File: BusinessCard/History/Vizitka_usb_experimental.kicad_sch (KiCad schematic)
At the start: 29 parts, among them J1 USB_B_Micro, J2 USB_C_Receptacle, J3 Conn_01x01

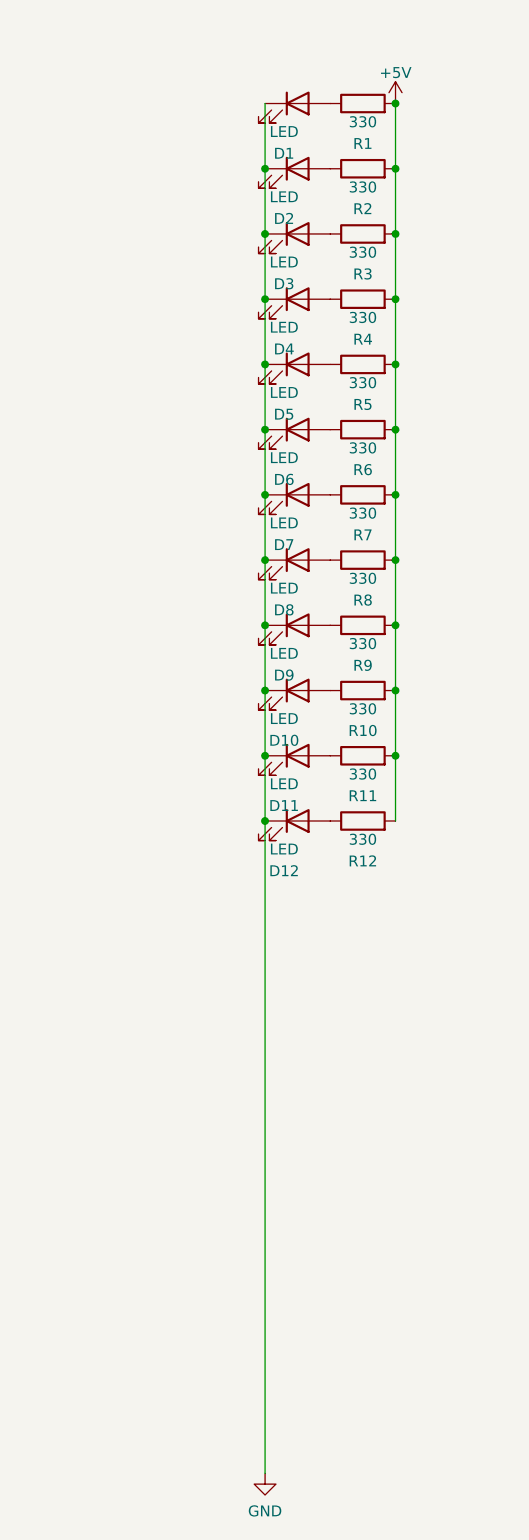
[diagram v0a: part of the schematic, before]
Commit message: Added aditional businesscards - Zuza, MichalModra...Actual Tapeout 2023-08-24, but repaired connection!
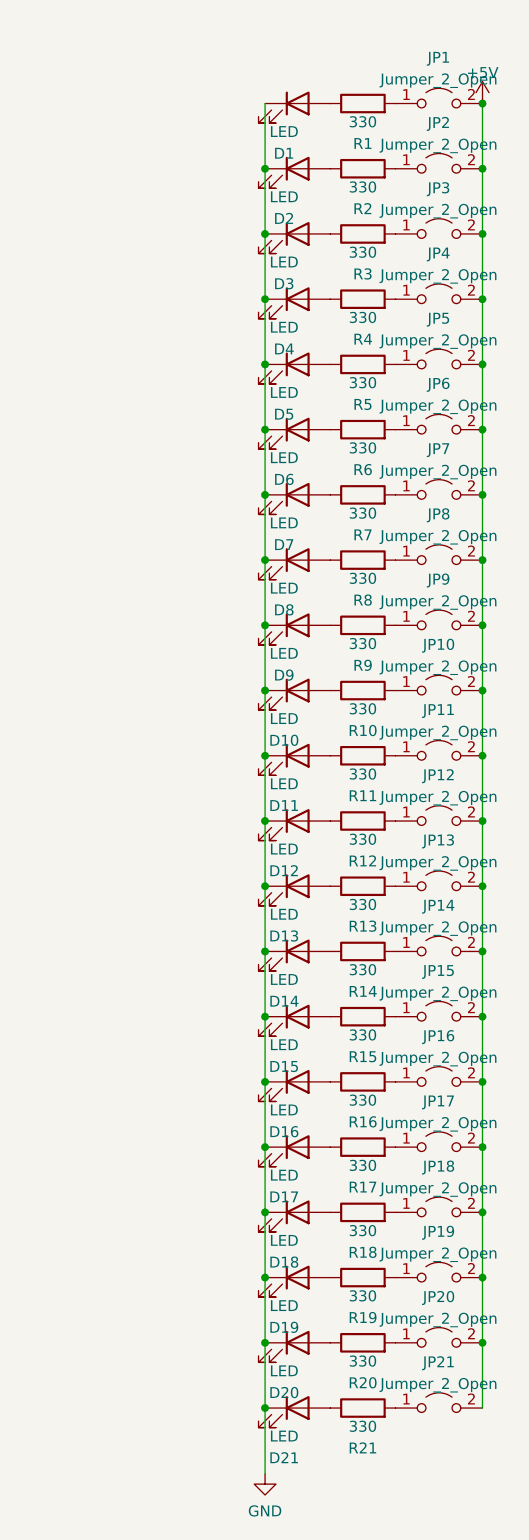
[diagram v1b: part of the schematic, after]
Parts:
- added D13, D14, D15, D16, D17, D18, D19, D20, D21: LED, meteopress:D_0802_side_woSilk, symbol Device:LED
- added JP1, JP10, JP11, JP12, JP13, JP14, JP15, JP16, JP17, JP18, JP19, JP2, JP20, JP21, JP3, JP4, JP5, JP6, JP7, JP8, JP9: Jumper_2_Open, Jumper:SolderJumper-2_P1.3mm_Open_TrianglePad1.0x1.5mm, symbol Jumper:Jumper_2_Open
- added R13, R14, R15, R16, R17, R18, R19, R20, R21: 330, meteopress:R_0201_woSilk, symbol Device:R
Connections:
- net +5V: now also JP1.2 (B), JP10.2 (B), JP11.2 (B), JP12.2 (B), JP13.2 (B), JP14.2 (B), JP15.2 (B), JP16.2 (B), JP17.2 (B), JP18.2 (B), JP19.2 (B), JP2.2 (B), JP20.2 (B), JP21.2 (B), JP3.2 (B), JP4.2 (B), JP5.2 (B), JP6.2 (B), JP7.2 (B), JP8.2 (B), JP9.2 (B); no longer R1.2, R10.2, R11.2, R12.2, R2.2, R3.2, R4.2, R5.2, R6.2, R7.2, R8.2, R9.2
- net GND: now also D13.1 (K), D14.1 (K), D15.1 (K), D16.1 (K), D17.1 (K), D18.1 (K), D19.1 (K), D20.1 (K), D21.1 (K)
- new net: JP14.1 (A), R14.2
- new net: JP1.1 (A), R1.2
- new net: JP12.1 (A), R12.2
- new net: JP20.1 (A), R20.2
- new net: JP3.1 (A), R3.2
- new net: JP2.1 (A), R2.2
- new net: D18.2 (A), R18.1
- new net: D17.2 (A), R17.1
- new net: JP17.1 (A), R17.2
- new net: JP5.1 (A), R5.2
- new net: JP7.1 (A), R7.2
- new net: JP10.1 (A), R10.2
- new net: JP9.1 (A), R9.2
- new net: D19.2 (A), R19.1
- new net: JP16.1 (A), R16.2
- new net: D16.2 (A), R16.1
- new net: D20.2 (A), R20.1
- new net: JP11.1 (A), R11.2
- new net: JP19.1 (A), R19.2
- new net: JP21.1 (A), R21.2
- new net: JP8.1 (A), R8.2
- new net: JP4.1 (A), R4.2
- new net: JP15.1 (A), R15.2
- new net: JP13.1 (A), R13.2
- new net: D14.2 (A), R14.1
- new net: D21.2 (A), R21.1
- new net: JP6.1 (A), R6.2
- new net: JP18.1 (A), R18.2
- new net: D13.2 (A), R13.1
- new net: D15.2 (A), R15.1
